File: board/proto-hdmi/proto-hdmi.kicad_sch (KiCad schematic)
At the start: 3 parts, among them J1 Conn_02x12_Odd_Even, J2 HDMI_A_1.4, U1 AMS1117-2.5

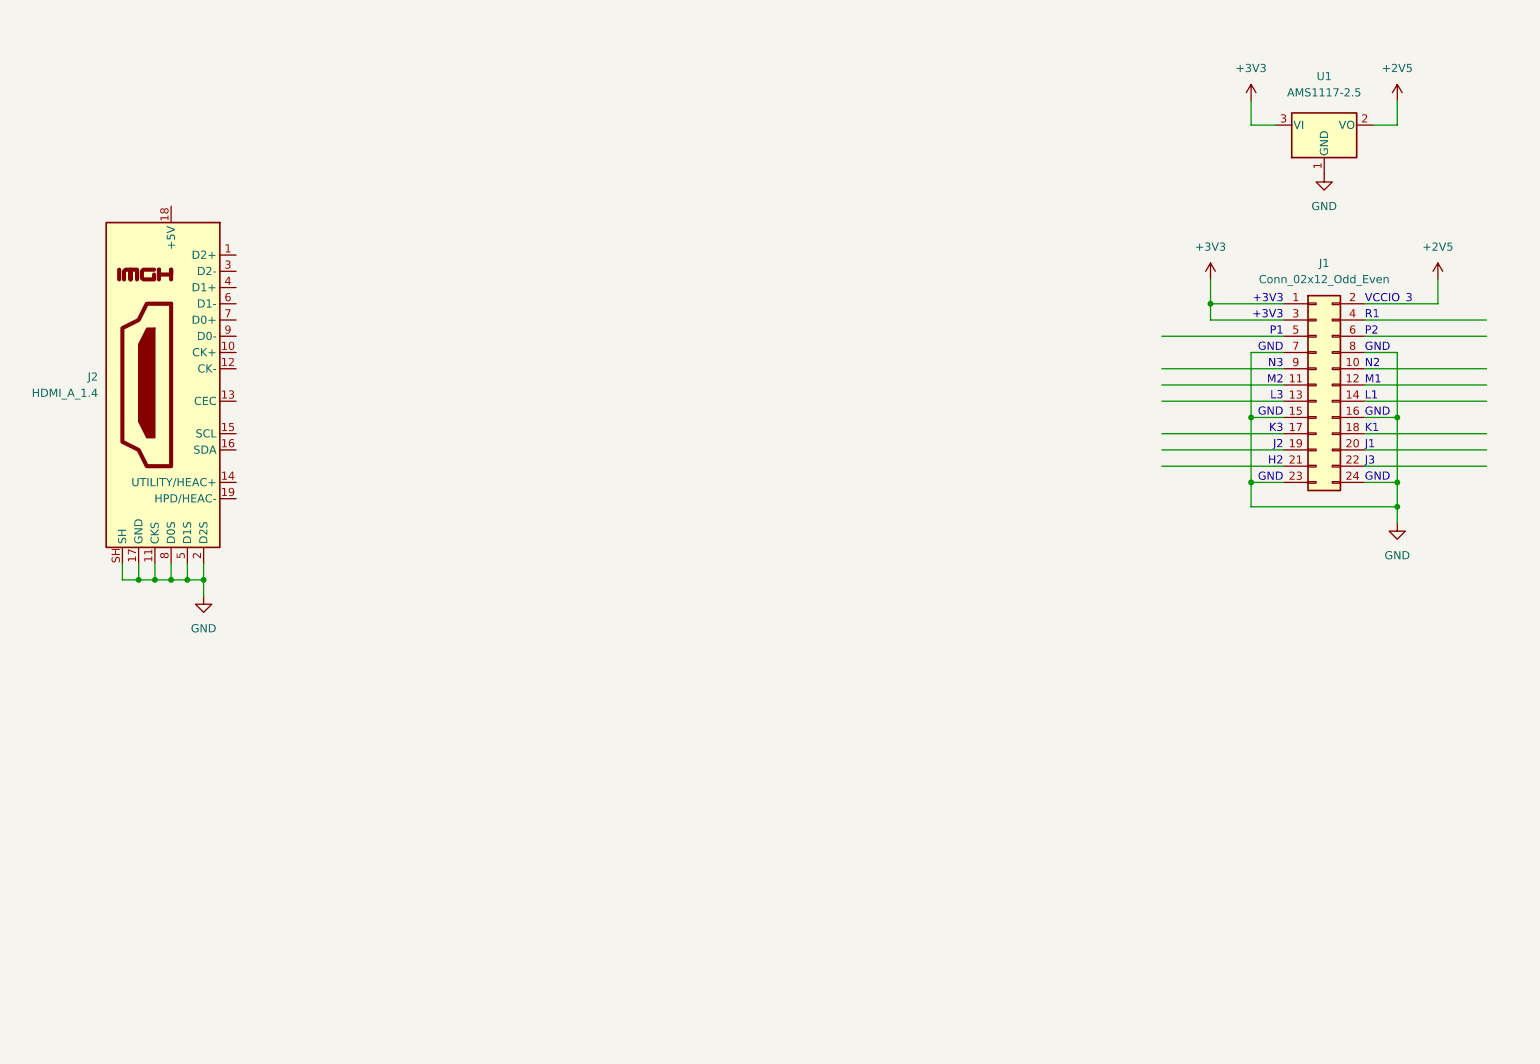
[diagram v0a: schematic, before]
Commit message: Route HDMI in resistor networks.
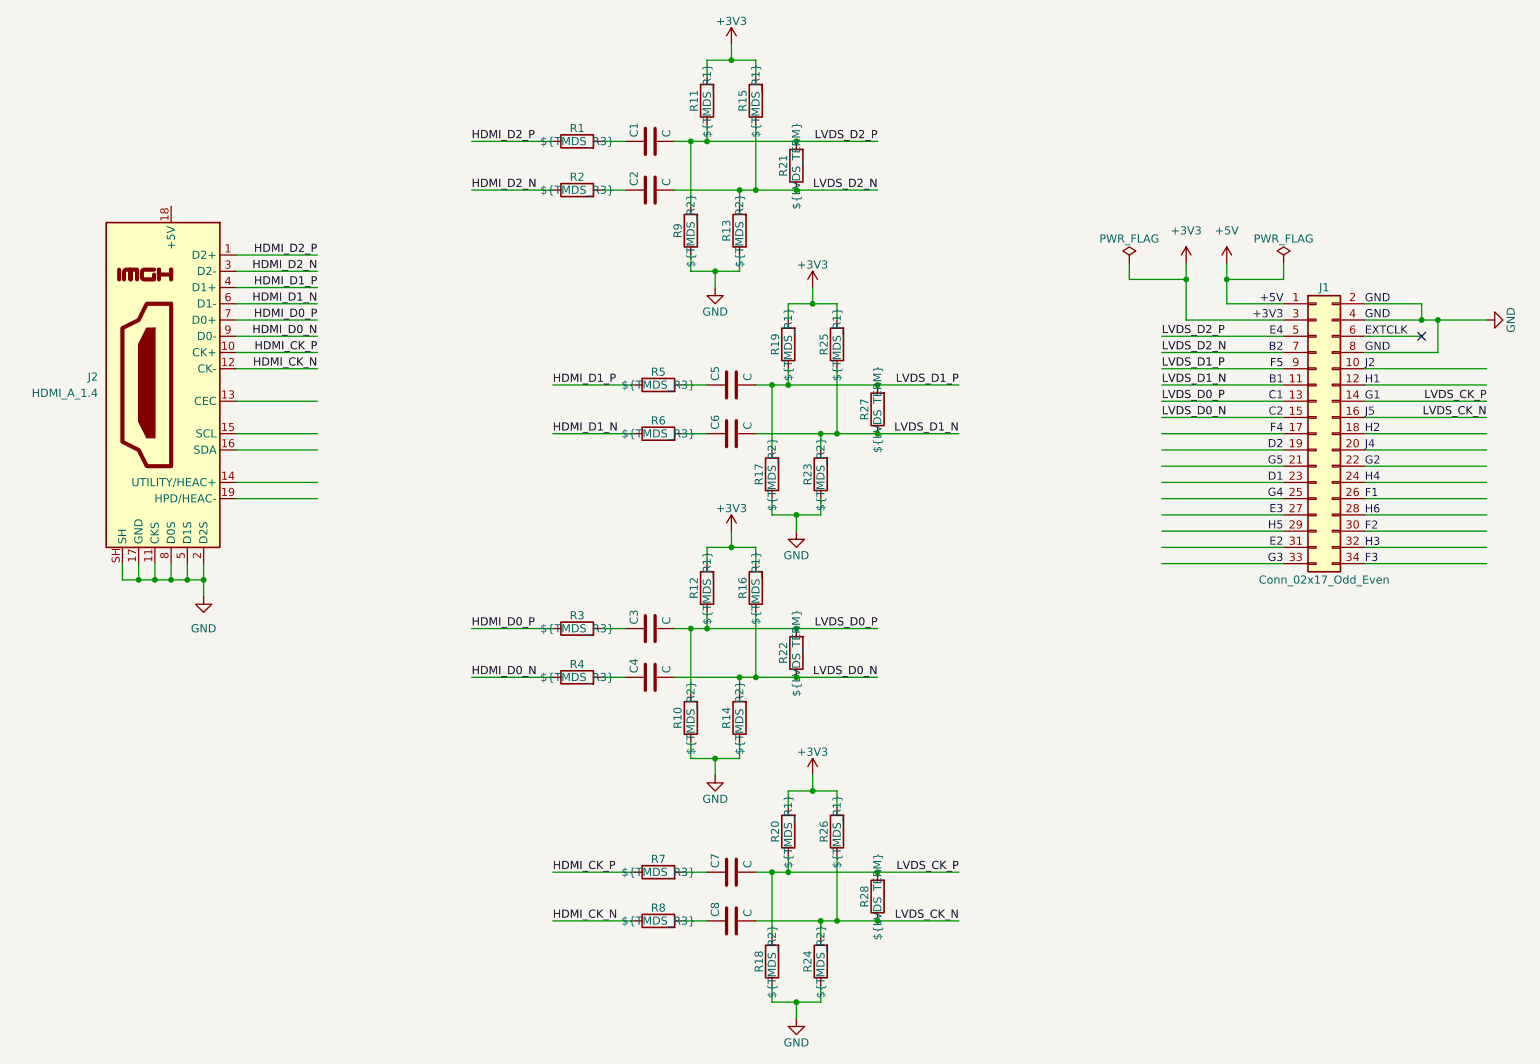
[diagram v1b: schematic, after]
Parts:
- removed J1: Conn_02x12_Odd_Even, Connector_PinSocket_2.54mm:PinSocket_2x12_P2.54mm_Horizontal, symbol Connector_Generic:Conn_02x12_Odd_Even
- removed U1: AMS1117-2.5, Package_TO_SOT_SMD:SOT-223-3_TabPin2, symbol Regulator_Linear:AMS1117-2.5
- added C1, C2, C3, C4, C5, C6, C7, C8: C, Capacitor_SMD:C_0402_1005Metric, symbol Device:C
- added J1: Conn_02x17_Odd_Even, Connector_PinSocket_2.54mm:PinSocket_2x17_P2.54mm_Horizontal, symbol Connector_Generic:Conn_02x17_Odd_Even
- added R1, R2, R3, R4, R5, R6, R7, R8: ${TMDS_R3}, Resistor_SMD:R_0402_1005Metric, symbol Device:R
- added R10, R13, R14, R17, R18, R23, R24, R9: ${TMDS_R2}, Resistor_SMD:R_0402_1005Metric, symbol Device:R
- added R11, R12, R15, R16, R19, R20, R25, R26: ${TMDS_R1}, Resistor_SMD:R_0402_1005Metric, symbol Device:R
- added R21, R22, R27, R28: ${LVDS_TERM}, Resistor_SMD:R_0402_1005Metric, symbol Device:R
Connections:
- net +3V3: now also J1.3 (Pin_3), R11.2, R12.2, R15.2, R16.2, R19.2, R20.2, R25.2, R26.2
- net GND: now also J1.2 (Pin_2), J1.4 (Pin_4), J1.8 (Pin_8), R10.1, R13.1, R14.1, R17.1, R18.1, R23.1, R24.1, R9.1
- net HDMI_D2_P: now reaches J2.1 (D2+)
- net HDMI_D2_P: now also R1.1
- net HDMI_CK_P: now reaches J2.10 (CK+)
- net HDMI_CK_P: now also R7.1
- net HDMI_CK_N: now reaches J2.12 (CK-)
- net HDMI_CK_N: now also R8.1
- net HDMI_D2_N: now reaches J2.3 (D2-)
- net HDMI_D2_N: now also R2.1
- net HDMI_D1_P: now reaches J2.4 (D1+)
- net HDMI_D1_P: now also R5.1
- net HDMI_D1_N: now reaches J2.6 (D1-)
- net HDMI_D1_N: now also R6.1
- net HDMI_D0_P: now reaches J2.7 (D0+)
- net HDMI_D0_P: now also R3.1
- net HDMI_D0_N: now reaches J2.9 (D0-)
- net HDMI_D0_N: now also R4.1
- new net: C6.1, R6.2
- new net: C5.1, R5.2
- new net: C2.1, R2.2
- new net: C7.1, R7.2
- new net: C8.1, R8.2
- new net: C1.1, R1.2
- new net: C4.1, R4.2
- new net: C3.1, R3.2
- new net +5V: J1.1 (Pin_1)
- new net LVDS_CK_N: C8.2, J1.16 (Pin_16), R24.2, R26.1, R28.1
- new net LVDS_CK_P: C7.2, J1.14 (Pin_14), R18.2, R20.1, R28.2
- new net LVDS_D0_N: C4.2, J1.15 (Pin_15), R14.2, R16.1, R22.1
- new net LVDS_D0_P: C3.2, J1.13 (Pin_13), R10.2, R12.1, R22.2
- new net LVDS_D1_N: C6.2, J1.11 (Pin_11), R23.2, R25.1, R27.1
- new net LVDS_D1_P: C5.2, J1.9 (Pin_9), R17.2, R19.1, R27.2
- new net LVDS_D2_N: C2.2, J1.7 (Pin_7), R13.2, R15.1, R21.1
- new net LVDS_D2_P: C1.2, J1.5 (Pin_5), R11.1, R21.2, R9.2
- no-connect marks 0 -> 1
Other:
- note added: "+5V"
- note added: "B1"
- note added: "B2"
- note added: "C1"
- note added: "C2"
- note added: "D1"
- note added: "D2"
- note added: "E2"
- note added: "E3"
- note added: "E4"
- note added: "EXTCLK"
- note added: "F1"
- note added: "F2"
- note added: "F3"
- note added: "F4"
- note added: "F5"
- note added: "G1"
- note added: "G2"
- note added: "G3"
- note added: "G4"
- note added: "G5"
- note added: "H1"
- note added: "H3"
- note added: "H4"
- note added: "H5"
- note added: "H6"
- note added: "J4"
- note added: "J5"
- note removed: "J1"
- note removed: "J3"
- note removed: "K1"
- note removed: "K3"
- note removed: "L1"
- note removed: "L3"
- note removed: "M1"
- note removed: "M2"
- note removed: "N2"
- note removed: "N3"
- note removed: "P1"
- note removed: "P2"
- note removed: "R1"
- note removed: "VCCIO_3"
